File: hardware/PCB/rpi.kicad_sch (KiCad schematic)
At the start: 0 parts

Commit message: Add more symbols and continue filling footprints
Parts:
- added J4: Conn_02x20_Odd_Even, symbol Connector_Generic:Conn_02x20_Odd_Even
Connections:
- new net +5V: J4.2 (Pin_2), J4.4 (Pin_4)
- new net GND: J4.14 (Pin_14), J4.20 (Pin_20), J4.25 (Pin_25), J4.30 (Pin_30), J4.34 (Pin_34), J4.39 (Pin_39), J4.6 (Pin_6), J4.9 (Pin_9)
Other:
- note added: "Topiary Trimbot - Raspberry Pi Connector"

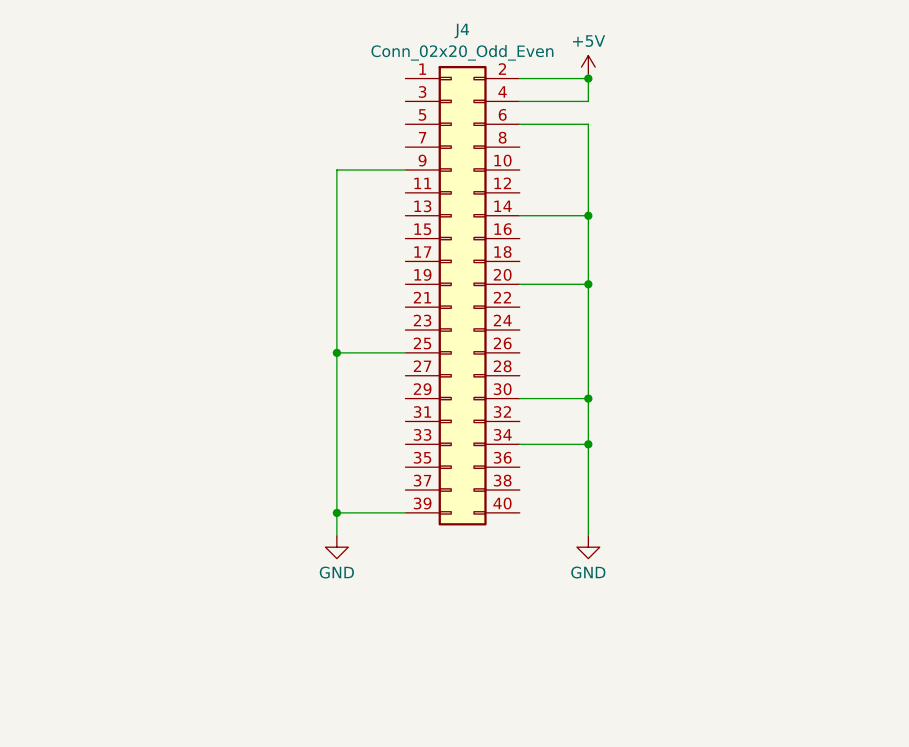
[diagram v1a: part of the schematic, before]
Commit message: Finished setting footprints for LCD, motors, RPi, and storage schematics
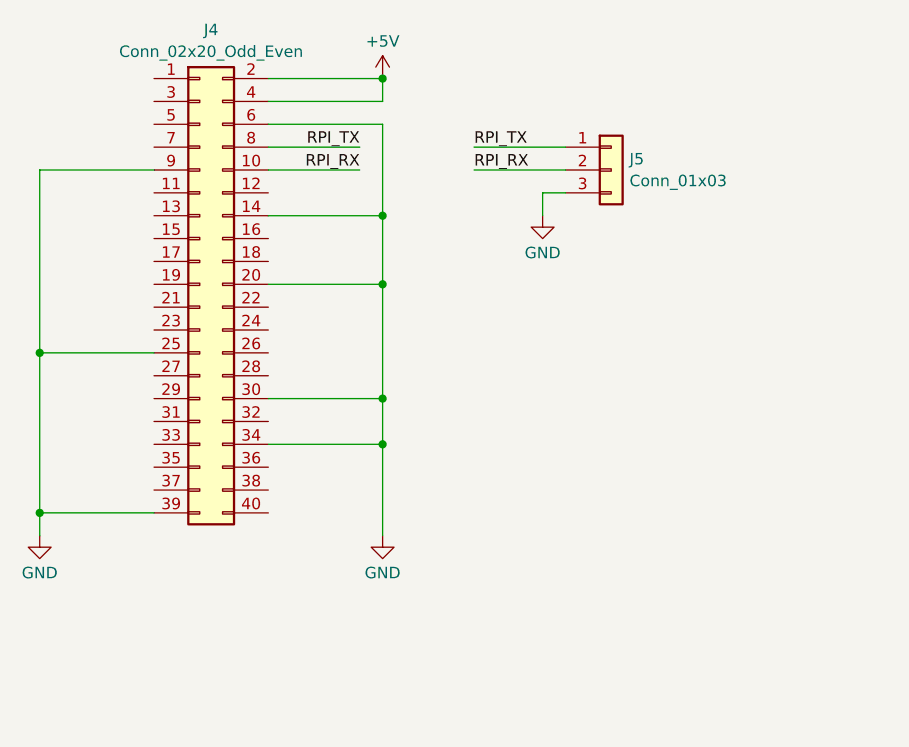
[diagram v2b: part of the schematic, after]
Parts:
- added J5: Conn_01x03, Connector_PinHeader_2.54mm:PinHeader_1x03_P2.54mm_Vertical, symbol Connector_Generic:Conn_01x03
- J4: footprint (none) -> Connector_IDC:IDC-Header_2x20_P2.54mm_Vertical
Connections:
- net GND: now also J5.3 (Pin_3)
- net RPI_RX: now reaches J4.10 (Pin_10)
- net RPI_RX: now also J5.2 (Pin_2)
- net RPI_TX: now reaches J4.8 (Pin_8)
- net RPI_TX: now also J5.1 (Pin_1)
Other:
- moved on the sheet: J4

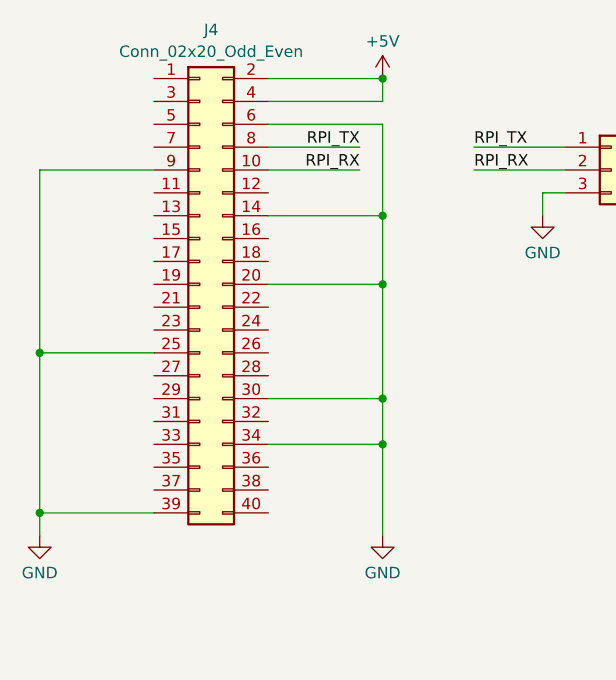
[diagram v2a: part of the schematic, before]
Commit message: Touch up some ERC violations
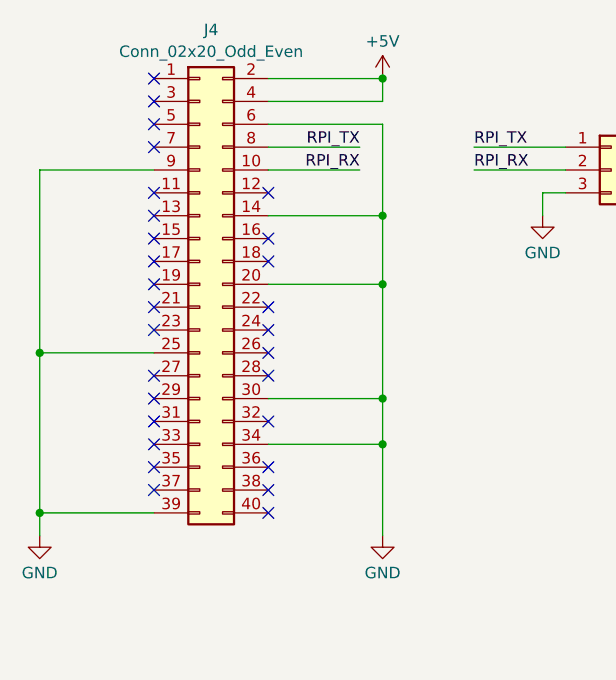
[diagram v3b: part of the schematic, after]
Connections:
- no-connect marks 0 -> 28
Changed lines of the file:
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@@
 		(color 0 0 0 0)
+	)
+	(no_connect
+		(at 68.58 116.84)
+	)
+	(no_connect
+		(at 81.28 101.6)
+	)
+	(no_connect
+		(at 81.28 106.68)
+	)
+	(no_connect
+		(at 68.58 109.22)
+	)
+	(no_connect
+		(at 81.28 93.98)
+	)
+	(no_connect
+		(at 81.28 119.38)
+	)
+	(no_connect
+		(at 68.58 104.14)
+	)
+	(no_connect
+		(at 81.28 121.92)
+	)
+	(no_connect
+		(at 68.58 101.6)
+	)
+	(no_connect
+		(at 81.28 114.3)
+	)
+	(no_connect
+		(at 68.58 96.52)
+	)
+	(no_connect
+		(at 81.28 96.52)
+	)
+	(no_connect
+		(at 81.28 124.46)
+	)
+	(no_connect
+		(at 68.58 114.3)
+	)
+	(no_connect
+		(at 68.58 88.9)
+	)
+	(no_connect
+		(at 68.58 93.98)
+	)
+	(no_connect
+		(at 68.58 91.44)
+	)
+	(no_connect
+		(at 68.58 76.2)
+	)
+	(no_connect
+		(at 81.28 109.22)
+	)
+	(no_connect
+		(at 68.58 99.06)
+	)
+	(no_connect
+		(at 81.28 104.14)
+	)
+	(no_connect
+		(at 68.58 119.38)
+	)
+	(no_connect
+		(at 81.28 88.9)
+	)
+	(no_connect
+		(at 68.58 111.76)
+	)
+	(no_connect
+		(at 68.58 121.92)
+	)
+	(no_connect
+		(at 68.58 78.74)
+	)
+	(no_connect
+		(at 68.58 83.82)
+	)
+	(no_connect
+		(at 68.58 81.28)
 	)
 	(wire

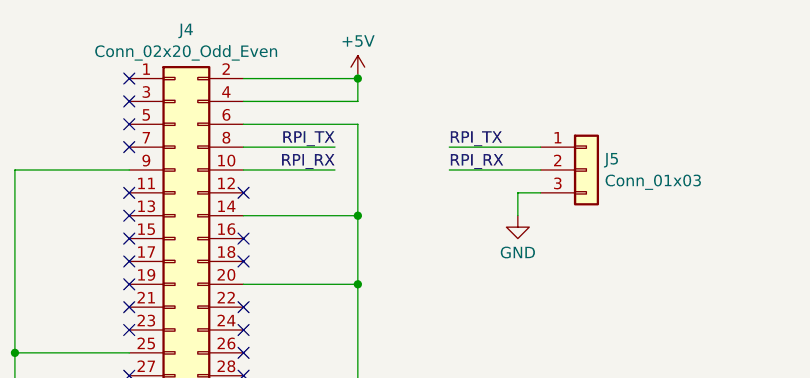
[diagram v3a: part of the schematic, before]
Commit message: Synchronized schematic draft and reannotated all
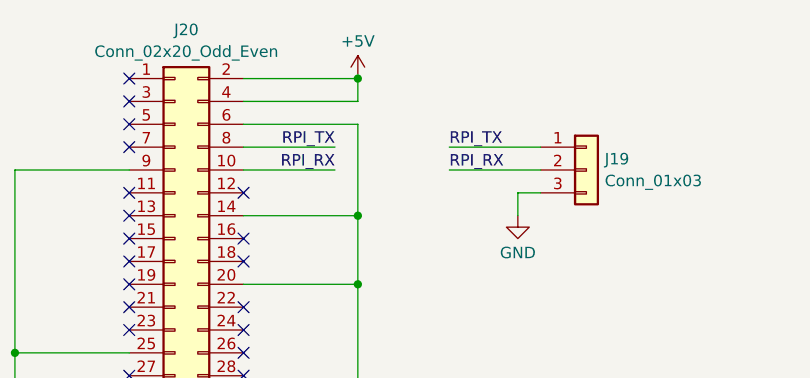
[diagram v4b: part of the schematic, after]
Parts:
- renumbered J5 to J19, J4 to J20
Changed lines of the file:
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@@
 			"BgAA4GHiLx2SpMhNGdD/2aBhL0k83e+xB4S8AIBHpOrStbKsE/qCQlPJDVt1Jea4lm4RAACAvzqC"
 			"kkikXt5ubQO9Yjr79ooViITN2g1CXgAAAAAA8HSDScoAAAAAAMBTDkJeAAAAAADwlIOQFwAAAAAA"
-			"POUg5AUAAAAAAE85CHkBAAAAAMBT7v8DJbGmJgTjOy8AAAAASUVORK5CYII="
+			"POUg5AUAAAAAAE85CHkBAAAAAMBT7v8DJbGmJgTjOy8AAAAASUVORK5CYIIAAAAAAAAAAAAAAAAA"
+			"AAAAAAAAAAAAAAAAAAAAAAAAAAAAAAAAAAAAAAAAAAAAAAAAAAAAAAAAAAAAAAAAAAAAAAAAAAAA"
+			"AAAAAAAAAAAAAAAAAAAAAAAAAAAAAAAAAAAAAAAAAAAAAAAAAAAAAAAAAAAAAAAAAAAAAAAAAAAA"
+			"AAAAAAAAAAAAAAAAAAAAAAAAAAAAAAAAAAAAAAAAAAAAAAAAAAAAAAAAAAAAAAAAAAAAAAAAAAAA"
+			"AAAAAAAAAAAAAAAAAAAAAAAAAAAAAAAAAAAAAAAAAAAAAAAAAAAAAAAAAAAAAAAAAAAAAAAAAAAA"
+			"AAAAAAAAAAAAAAAAAAAAAAAAAAAAAAAAAAAAAAAAAAAAAAAAAAAAAAAAAAAAAAAAAAAAAAAAAAAA"
+			"AAAAAAAAAAAAAAAAAAAAAAAAAAAAAAAAAAAAAAAAAAAAAAAAAAAAAAAAAAAAAAAAAAAAAAAAAAAA"
+			"AAAAAAAAAAAAAAAAAAAAAAAAAAAAAAAAAAAAAAAAAAAAAAAAAAAAAAAAAAAAAAAAAAAAAAAAAAAA"
+			"AAAAAAAAAAAAAAAAAAAAAAAAAAAAAAAAAAAAAAAAAAAAAAAAAAAAAAAAAAAAAAAAAAAAAAAAAAAA"
+			"AAAAAAAAAAAAAAAAAAAAAAAAAAAAAAAAAAAAAAAAAAAAAAAAAAAAAAAAAAAAAAAAAAAAAAAAAAAA"
+			"AAAAAAAAAAAAAAAAAAAAAAAAAAAAAAAAAAAAAAAAAAAAAAAAAAAAAAAAAAAAAAAAAAAAAAAAAAAA"
+			"AAAAAAAAAAAAAAAAAAAAAAAAAAAAAAAAAAAAAAAAAAAAAAAAAAAAAAAAAAAAAAAAAAAAAAAAAAAA"
+			"AAAAAAAAAAAAAAAAAAAAAAAAAAAAAAAAAAAAAAAAAAAAAAAAAAAAAAAAAAAAAAAAAAAAAAAAAAAA"
+			"AAAAAAAAAAAAAAAAAAAAAAAAAAAAAAAAAAAAAAAAAAAAAAAAAAAAAAAAAAAAAAAAAAAAAAAAAAAA"
+			"AAAAAAAAAAAAAAAAAAAAAAAAAAAAAAAAAAAAAAAAAAAAAAAAAAAAAAAAAAAAAAAAAAAAAAAAAAAA"
+			"AAAAAAAAAAAAAAAAAAAAAAAAAAAAAAAAAAAAAAAAAAAAAAAAAAAAAAAAAAAAAAAAAAAAAAAAAAAA"
+			"AAAAAAAAAAAAAAAAAAAAAAAAAAAAAAAAAAAAAAAAAAAAAAAAAAAAAAAAAAAAAAAAAAAAAAAAAAAA"
+			"AAAAAAAAAAAAAAAAAAAAAAAAAAAAAAAAAAAAAAAAAAAAAAAAAAAAAAAAAAAAAAAAAAAAAAAAAAAA"
+			"AAAAAAAAAAAAAAAAAAAAAAAAAAAAAAAAAAAAAAAAAAAAAAAAAAAAAAAAAA=="
 		)
 	)
@@
 		(dnp no)
 		(fields_autoplaced yes)
-		(property "Reference" "J5"
+		(property "Reference" "J19"
 			(at 121.412 85.1478 0)
 			(effects
@@
 			(project ""
 				(path "/2826ff7c-9767-4078-8ea2-1cd3a432abf3/c95f1fc4-1ba1-4ddd-af2e-ed3477b5512d"
-					(reference "J5")
+					(reference "J19")
 					(unit 1)
 				)
@@
 		(dnp no)
 		(fields_autoplaced yes)
-		(property "Reference" "#PWR065"
+		(property "Reference" "#PWR0136"
 			(at 93.98 80.01 0)
 			(effects
@@
 			(project ""
 				(path "/2826ff7c-9767-4078-8ea2-1cd3a432abf3/c95f1fc4-1ba1-4ddd-af2e-ed3477b5512d"
-					(reference "#PWR065")
+					(reference "#PWR0136")
 					(unit 1)
 				)
@@
 		(dnp no)
 		(fields_autoplaced yes)
-		(property "Reference" "#PWR066"
+		(property "Reference" "#PWR0139"
 			(at 93.98 133.35 0)
 			(effects
@@
 			(project ""
 				(path "/2826ff7c-9767-4078-8ea2-1cd3a432abf3/c95f1fc4-1ba1-4ddd-af2e-ed3477b5512d"
-					(reference "#PWR066")
+					(reference "#PWR0139")
 					(unit 1)
 				)
@@
 		(dnp no)
 		(fields_autoplaced yes)
-		(property "Reference" "#PWR068"
+		(property "Reference" "#PWR0137"
 			(at 111.76 97.79 0)
 			(effects
@@
 			(project "TopiaryTrimbot"
 				(path "/2826ff7c-9767-4078-8ea2-1cd3a432abf3/c95f1fc4-1ba1-4ddd-af2e-ed3477b5512d"
-					(reference "#PWR068")
+					(reference "#PWR0137")
 					(unit 1)
 				)
@@
 		(dnp no)
 		(fields_autoplaced yes)
-		(property "Reference" "#PWR067"
+		(property "Reference" "#PWR0138"
 			(at 55.88 133.35 0)
 			(effects
@@
 			(project "TopiaryTrimbot"
 				(path "/2826ff7c-9767-4078-8ea2-1cd3a432abf3/c95f1fc4-1ba1-4ddd-af2e-ed3477b5512d"
-					(reference "#PWR067")
+					(reference "#PWR0138")
 					(unit 1)
 				)
@@
 		(dnp no)
 		(fields_autoplaced yes)
-		(property "Reference" "J4"
+		(property "Reference" "J20"
 			(at 74.93 70.7855 0)
 			(effects
@@
 			(project ""
 				(path "/2826ff7c-9767-4078-8ea2-1cd3a432abf3/c95f1fc4-1ba1-4ddd-af2e-ed3477b5512d"
-					(reference "J4")
+					(reference "J20")
 					(unit 1)
 				)

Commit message: Finish first pass placement of parts on PCB, several updates and fixes to schematic included
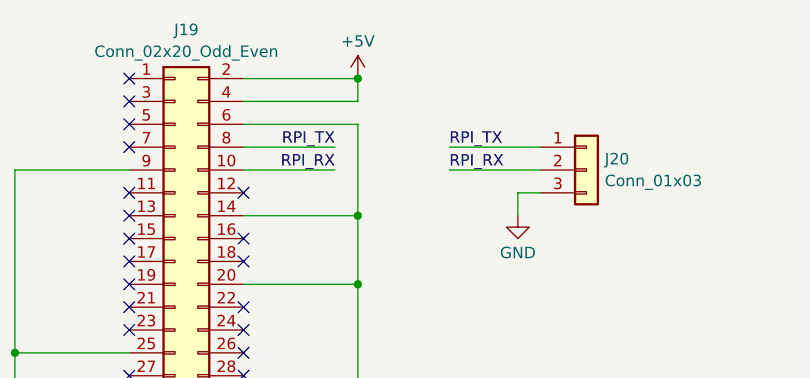
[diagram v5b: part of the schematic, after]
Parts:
- renumbered J20 to J19, J19 to J20
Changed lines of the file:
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@@
 		(dnp no)
 		(fields_autoplaced yes)
-		(property "Reference" "J19"
+		(property "Reference" "J20"
 			(at 121.412 85.1478 0)
 			(effects
@@
 			(project ""
 				(path "/2826ff7c-9767-4078-8ea2-1cd3a432abf3/c95f1fc4-1ba1-4ddd-af2e-ed3477b5512d"
-					(reference "J19")
+					(reference "J20")
 					(unit 1)
 				)
@@
 		(dnp no)
 		(fields_autoplaced yes)
-		(property "Reference" "#PWR0136"
+		(property "Reference" "#PWR0139"
 			(at 93.98 80.01 0)
 			(effects
@@
 			(project ""
 				(path "/2826ff7c-9767-4078-8ea2-1cd3a432abf3/c95f1fc4-1ba1-4ddd-af2e-ed3477b5512d"
-					(reference "#PWR0136")
+					(reference "#PWR0139")
 					(unit 1)
 				)
@@
 		(dnp no)
 		(fields_autoplaced yes)
-		(property "Reference" "#PWR0139"
+		(property "Reference" "#PWR0140"
 			(at 93.98 133.35 0)
 			(effects
@@
 			(project ""
 				(path "/2826ff7c-9767-4078-8ea2-1cd3a432abf3/c95f1fc4-1ba1-4ddd-af2e-ed3477b5512d"
-					(reference "#PWR0139")
+					(reference "#PWR0140")
 					(unit 1)
 				)
@@
 		(dnp no)
 		(fields_autoplaced yes)
-		(property "Reference" "#PWR0137"
+		(property "Reference" "#PWR0141"
 			(at 111.76 97.79 0)
 			(effects
@@
 			(project "TopiaryTrimbot"
 				(path "/2826ff7c-9767-4078-8ea2-1cd3a432abf3/c95f1fc4-1ba1-4ddd-af2e-ed3477b5512d"
-					(reference "#PWR0137")
+					(reference "#PWR0141")
 					(unit 1)
 				)
@@
 		(dnp no)
 		(fields_autoplaced yes)
-		(property "Reference" "J20"
+		(property "Reference" "J19"
 			(at 74.93 70.7855 0)
 			(effects
@@
 			(project ""
 				(path "/2826ff7c-9767-4078-8ea2-1cd3a432abf3/c95f1fc4-1ba1-4ddd-af2e-ed3477b5512d"
-					(reference "J20")
-					(unit 1)
-				)
+					(reference "J19")
+					(unit 1)
+				)

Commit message: all part numbers
may need revisions
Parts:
- J19: MANUFACTURER (none) -> Sullins; Manufacturer_Part_Number (none) -> SBH11-PBPC-D10-ST-BK
- J20: MANUFACTURER (none) -> Wurth; Manufacturer_Part_Number (none) -> 61201021621
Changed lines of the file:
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@@
+			)
+		)
+		(property "MANUFACTURER" "Wurth"
+			(at 119.38 86.36 0)
+			(effects
+				(font
+					(size 1.27 1.27)
+				)
+				(hide yes)
+			)
+		)
+		(property "Manufacturer_Part_Number" "61201021621"
+			(at 119.38 86.36 0)
+			(effects
+				(font
+					(size 1.27 1.27)
+				)
+				(hide yes)
 			)
 		)
@@
 			(at 73.66 99.06 0)
 			(effects
+				(font
+					(size 1.27 1.27)
+				)
+				(hide yes)
+			)
+		)
+		(property "MANUFACTURER" "Sullins"
+			(at 73.66 99.06 0)
+			(effects
+				(font
+					(size 1.27 1.27)
+				)
+				(hide yes)
+			)
+		)
+		(property "Manufacturer_Part_Number" "SBH11-PBPC-D10-ST-BK"
+			(at 73.66 99.06 0)
+			(effects
